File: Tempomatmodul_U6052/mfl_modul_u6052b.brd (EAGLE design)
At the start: 78 x 58 mm, 27 parts, among them IC1 U6052B-A, J1 43045-0800, K1 APF30212C, K2 APF30212C, K3 APF30212C, K4 APF30212C

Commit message: Fixed. Running version!
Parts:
- removed D6: P6KEXXC, diode:CB417-15
- removed R11, R12: 665, rcl:0207/7
- removed R13: 931, rcl:0207/7
- added C3: 100nF, rcl:C025-025X050
- added LED1: led grün 2,2v 20mA, led:LED3MM
- C1: value 100µF -> 1nF
- C2: value 1nF -> 100uF/36V; device rcl:C025-025X050 -> rcl:E2,5-6
- D1: value BYW52 -> EP20D; device diode:DO204-10 -> diode:DO15-12
- D2, D3, D4, D5: value CGRM4004-G -> MBSR140; device diode:SOD-123_MINI-SMA -> Heinrich:DO214AA
- J1: value 43045-0800 -> 39-30-1100; device Heinrich:43045-0800 -> Heinrich:39-30-1100
- R1: value 100 -> 560
- R10: value 200 -> 510
- R2: value 510 -> 100
- R3: value 200 -> 200k
- R4: value 270k -> 200
- R5: value 20k -> 931
- R6: value 150k -> 665
- R7: value 39k -> 665
- R8: value 200k -> 200
- R9: value 66.5 -> 66,5
- moved R8 67.8 mm to (69.8, 51.4), turned to 90 degrees
- moved R10 53.2 mm to (33.0, 16.5), turned to 0 degrees
- moved R3 44.2 mm to (56.5, 7.62), turned to 0 degrees
- moved R1 41.3 mm to (69.8, 17.8), turned to 90 degrees
- moved R5 38.1 mm to (39.4, 44.5), turned to 270 degrees
- moved R7 33.9 mm to (47.0, 51.4), turned to 90 degrees
- moved R6 32.0 mm to (62.2, 51.4), turned to 90 degrees
- moved C1 31.8 mm to (54.6, 23.5), turned to 0 degrees
- moved R4 27.6 mm to (33.0, 9.53), turned to 0 degrees
- moved R2 23.9 mm to (45.7, 23.5), turned to 0 degrees
- moved IC1 21.9 mm to (50.8, 16.5), turned to 180 degrees
- moved D1 14.9 mm to (24.8, 24.8), turned to 270 degrees
- moved C2 11.7 mm to (33.0, 22.2), turned to 180 degrees
- moved R9 11.4 mm to (54.6, 51.4)
- moved J1 6.35 mm to (0.00, 33.0)
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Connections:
- net K1 renamed PLUS
- net K2 renamed ABRUF
- net K3 renamed MINUS
- net K4 renamed I/O
- removed net +12V: D1.C, D2.C, D3.C, D4.C, D5.C, K1.2, K2.2, K3.2, K4.2, R2.1, R3.1, R4.1, R6.1
- removed net LD: IC1.15, R4.2, R5.2
- removed net MFL_CC: J1.5, R1.1
- removed net N$6: K1.NO, K2.NO, K3.NO, K4.NC, R11.1, R13.2
- removed net N$8: K2.COM, R10.1
- removed net PO: IC1.3, R6.2, R7.2
- new net IBUS: J1.3, J1.4
- new net MFL: J1.6, R2.1
- new net N$10: K2.COM, R8.1
- new net N$11: K3.COM, R7.1
- new net N$12: K1.NO, K2.NO, K3.NO, K4.NC, R5.2, R6.1
- new net N$3: LED1.A, R1.1
- new net VCC: D1.C, D2.C, D3.C, D4.C, D5.C, K1.2, K2.2, K3.2, K4.2, R1.2, R10.1, R4.1
- net EML1: now also J1.5, R6.2, R7.2, R8.2; no longer J1.8, R10.2, R11.2, R12.2
- net EML2: now also J1.10, R5.1; no longer J1.4, R13.1
- net GND: now also C2.-, C3.2, IC1.15, IC1.3, J1.7, J1.8, J1.9; no longer C2.2, D6.A, J1.2, J1.3, R5.1, R7.1
- net N$1: now also R2.2; no longer R1.2
- net N$2: now also R4.2; no longer R3.2
- net N$4: now also IC1.18, LED1.K; no longer K3.COM, R12.1
- net OSC: now also C1.1, R3.2; no longer C2.1, R8.2
- net VBAT: now also J1.1, J1.2; no longer D6.C, J1.6, J1.7
- net VS: now also C2.+, C3.1, R10.2; no longer C1.1, R2.2
- net VSTAB: now also R3.1; no longer R8.1
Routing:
- net VCC: track 0.00 -> 123.5 mm
- net +12V: track 104.3 -> 0.00 mm
- net N$12: track 0.00 -> 39.6 mm
- net ABRUF: track 49.7 -> 12.1 mm
- net LD: track 35.0 -> 0.00 mm, vias 1 -> 0
- net N$6: track 34.5 -> 0.00 mm
- net PLUS: track 41.7 -> 9.04 mm
- net MFL: track 0.00 -> 23.0 mm
- net PO: track 21.8 -> 0.00 mm
- net MINUS: track 42.3 -> 20.7 mm
- net MFL_CC: track 17.4 -> 0.00 mm
- net I/O: track 26.5 -> 9.45 mm
- net N$2: track 27.7 -> 11.7 mm
- net EML2: track 45.4 -> 29.8 mm, vias 1 -> 0
- net VBAT: track 12.7 -> 20.5 mm
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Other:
- board text added: "BMW MFL Dekoder für BMW E31 / M70 Heinrich Geiger für www.8er.org"
- board text removed: "8-Bit MFL Dekoder für BMW E31 / M70 Heinrich Geiger (c) www.8er.org"

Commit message: Fosc corrected
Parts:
- C1: value 1nF -> 680pF
- R3: value 200k -> 69k6
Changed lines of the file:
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@@
 </autorouter>
 <elements>
-<element name="C1" library="rcl" library_urn="urn:adsk.eagle:library:334" package="C025-025X050" package3d_urn="urn:adsk.eagle:package:23629/2" value="1nF" x="54.61" y="23.495" smashed="yes">
+<element name="C1" library="rcl" library_urn="urn:adsk.eagle:library:334" package="C025-025X050" package3d_urn="urn:adsk.eagle:package:23629/2" value="680pF" x="54.61" y="23.495" smashed="yes">
 <attribute name="NAME" x="58.801" y="22.479" size="1.27" layer="25" font="vector" ratio="15" rot="R90"/>
 <attribute name="SPICEPREFIX" value="C" x="54.61" y="23.495" size="1.778" layer="27" display="off"/>
@@
 <attribute name="SPICEPREFIX" value="R" x="45.72" y="23.495" size="1.778" layer="27" display="off"/>
 </element>
-<element name="R3" library="rcl" library_urn="urn:adsk.eagle:library:334" package="0207/7" package3d_urn="urn:adsk.eagle:package:23493/1" value="200k" x="56.515" y="7.62" smashed="yes">
+<element name="R3" library="rcl" library_urn="urn:adsk.eagle:library:334" package="0207/7" package3d_urn="urn:adsk.eagle:package:23493/1" value="69k6" x="56.515" y="7.62" smashed="yes">
 <attribute name="NAME" x="62.738" y="6.35" size="1.27" layer="25" font="vector" ratio="15" rot="R90"/>
 <attribute name="SPICEPREFIX" value="R" x="56.515" y="7.62" size="1.778" layer="27" display="off"/>

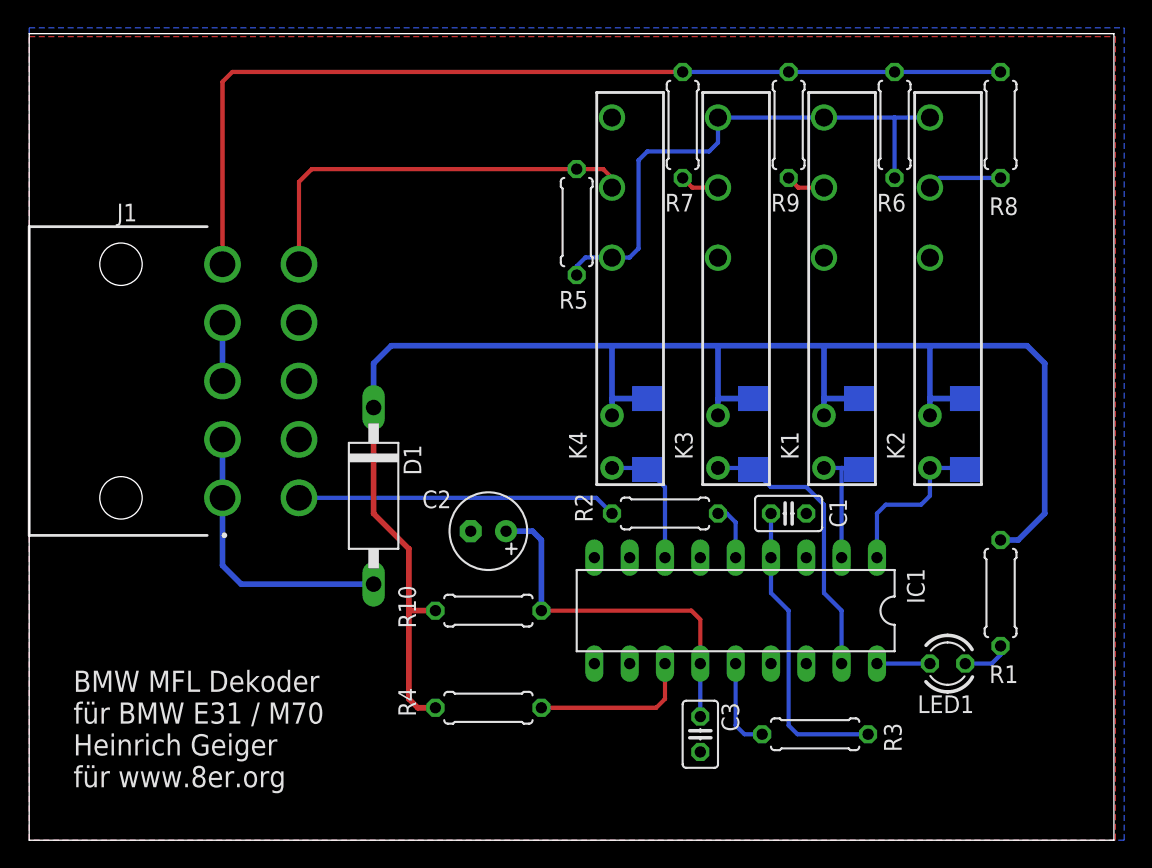
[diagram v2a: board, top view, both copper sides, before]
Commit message: Added support for V8 engines (M60 and M62)
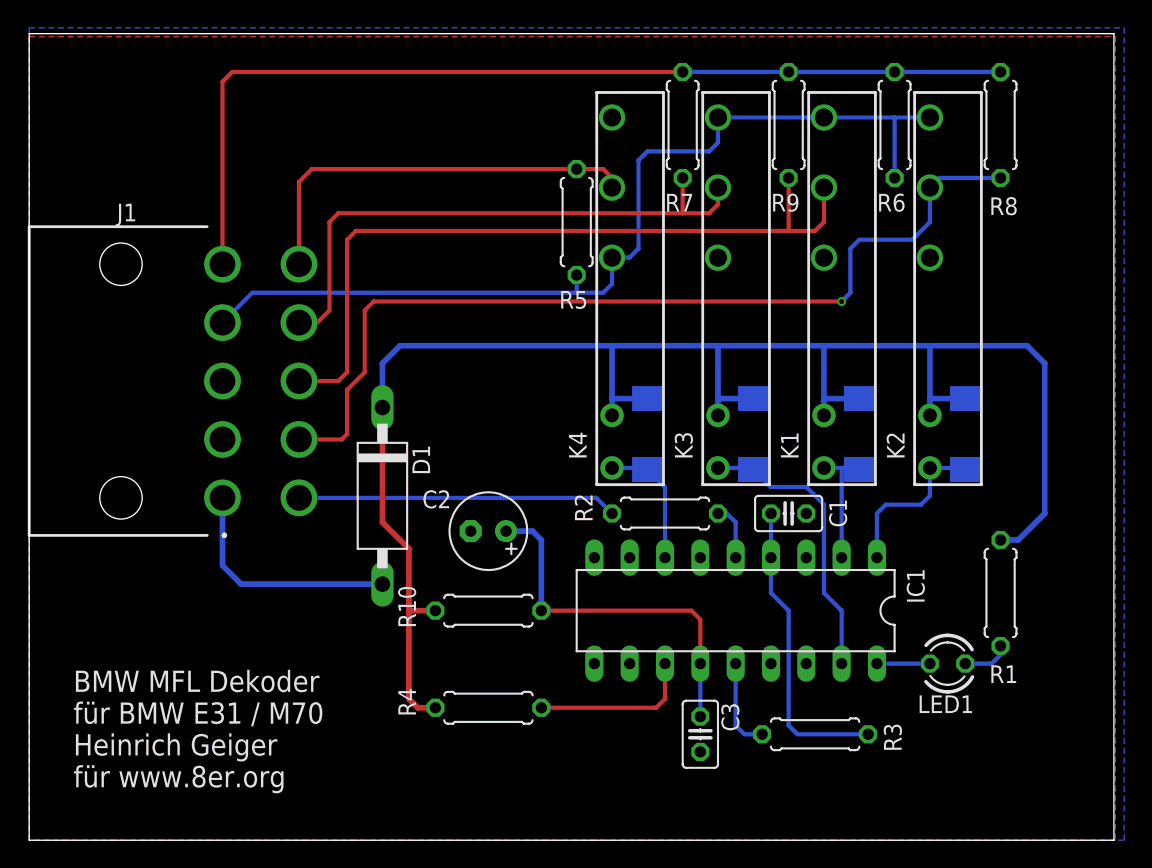
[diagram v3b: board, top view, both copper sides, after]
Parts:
- moved D1 0.63 mm to (25.4, 24.8)
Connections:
- net EML2 renamed EML2/X72.4
- removed net IBUS: J1.3, J1.4
- removed net N$10: K2.COM, R8.1
- removed net N$11: K3.COM, R7.1
- removed net N$12: K1.NO, K2.NO, K3.NO, K4.NC, R5.2, R6.1
- removed net N$9: K1.COM, R9.1
- new net X72.1: J1.4, K1.NO, K2.NO, K3.NO, K4.NC, R5.2, R6.1
- new net X72.2: J1.7, K2.COM, R8.1
- new net X72.3: J1.9, K3.COM, R7.1
- new net X72.7: J1.8, K1.COM, R9.1
- net GND: now also J1.2; no longer J1.7, J1.8, J1.9
- net VBAT: no longer J1.2
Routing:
- net X72.1: track 0.00 -> 68.5 mm
- net X72.2: track 0.00 -> 66.0 mm, vias 0 -> 1
- net X72.7: track 0.00 -> 54.4 mm
- net X72.3: track 0.00 -> 41.1 mm
- net N$12: track 39.6 -> 0.00 mm
- net N$10: track 5.37 -> 0.00 mm
- net IBUS: track 4.20 -> 0.00 mm
- net VBAT: track 20.5 -> 16.9 mm
- net N$9: track 2.83 -> 0.00 mm
- net N$11: track 2.83 -> 0.00 mm
- net VCC: track 123.5 -> 122.6 mm
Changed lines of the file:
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@@
 <attribute name="SPICEPREFIX" value="C" x="33.02" y="22.225" size="1.778" layer="27" rot="R180" display="off"/>
 </element>
-<element name="D1" library="diode" library_urn="urn:adsk.eagle:library:210" package="DO15-12" package3d_urn="urn:adsk.eagle:package:43369/1" value="EP20D" x="24.765" y="24.765" smashed="yes" rot="R270">
-<attribute name="NAME" x="26.924" y="28.448" size="1.27" layer="25" font="vector" ratio="15" rot="R270"/>
+<element name="D1" library="diode" library_urn="urn:adsk.eagle:library:210" package="DO15-12" package3d_urn="urn:adsk.eagle:package:43369/1" value="EP20D" x="25.4" y="24.765" smashed="yes" rot="R270">
+<attribute name="NAME" x="27.559" y="28.448" size="1.27" layer="25" font="vector" ratio="15" rot="R270"/>
 </element>
 <element name="D2" library="Heinrich" package="DO214AA" value="MBSR140" x="59.69" y="29.21" smashed="yes" rot="MR270">
@@
 <vertex x="0" y="0"/>
 </polygon>
-<contactref element="J1" pad="7"/>
-<contactref element="J1" pad="9"/>
-<contactref element="J1" pad="8"/>
 <contactref element="C3" pad="2"/>
+<contactref element="J1" pad="2"/>
 </signal>
 <signal name="N$1">
@@
 <contactref element="K4" pad="2"/>
 <contactref element="R1" pad="2"/>
-<wire x1="24.765" y1="31.115" x2="24.765" y2="34.29" width="0.4064" layer="16"/>
-<wire x1="24.765" y1="34.29" x2="26.035" y2="35.56" width="0.4064" layer="16"/>
+<wire x1="25.4" y1="31.115" x2="25.4" y2="34.29" width="0.4064" layer="16"/>
+<wire x1="25.4" y1="34.29" x2="26.67" y2="35.56" width="0.4064" layer="16"/>
 <wire x1="71.755" y1="35.56" x2="73.025" y2="34.29" width="0.4064" layer="16"/>
-<wire x1="26.035" y1="35.56" x2="41.91" y2="35.56" width="0.4064" layer="16"/>
+<wire x1="26.67" y1="35.56" x2="41.91" y2="35.56" width="0.4064" layer="16"/>
 <wire x1="41.91" y1="35.56" x2="49.53" y2="35.56" width="0.4064" layer="16"/>
 <wire x1="49.53" y1="35.56" x2="57.15" y2="35.56" width="0.4064" layer="16"/>
@@
 <wire x1="64.78" y1="31.76" x2="64.77" y2="31.75" width="0.4064" layer="16"/>
 <wire x1="73.025" y1="34.29" x2="73.025" y2="23.495" width="0.4064" layer="16"/>
-<wire x1="24.765" y1="31.115" x2="24.765" y2="23.495" width="0.4064" layer="1"/>
+<wire x1="25.4" y1="31.115" x2="25.4" y2="22.86" width="0.4064" layer="1"/>
 <wire x1="27.305" y1="20.955" x2="27.305" y2="16.51" width="0.4064" layer="1"/>
-<wire x1="24.765" y1="23.495" x2="27.305" y2="20.955" width="0.4064" layer="1"/>
+<wire x1="25.4" y1="22.86" x2="27.305" y2="20.955" width="0.4064" layer="1"/>
 <wire x1="29.21" y1="16.51" x2="27.305" y2="16.51" width="0.4064" layer="1"/>
 <wire x1="27.305" y1="10.16" x2="27.94" y2="9.525" width="0.4064" layer="1"/>
@@
 <contactref element="D1" pad="A"/>
 <contactref element="J1" pad="1"/>
-<contactref element="J1" pad="2"/>
 <wire x1="13.9" y1="24.62" x2="13.9" y2="19.755" width="0.4064" layer="16"/>
 <wire x1="13.9" y1="19.755" x2="15.24" y2="18.415" width="0.4064" layer="16"/>
-<wire x1="15.24" y1="18.415" x2="24.765" y2="18.415" width="0.4064" layer="16"/>
-<wire x1="13.9" y1="24.62" x2="13.9" y2="28.82" width="0.4064" layer="16"/>
+<wire x1="15.24" y1="18.415" x2="25.4" y2="18.415" width="0.4064" layer="16"/>
 </signal>
 <signal name="MFL">
@@
 <wire x1="14.605" y1="55.245" x2="46.99" y2="55.245" width="0.3048" layer="1"/>
 </signal>
-<signal name="N$9">
+<signal name="X72.7">
 <contactref element="R9" pad="1"/>
 <contactref element="K1" pad="COM"/>
-<wire x1="57.15" y1="46.93" x2="55.305" y2="46.93" width="0.3048" layer="1"/>
-<wire x1="55.305" y1="46.93" x2="54.61" y2="47.625" width="0.3048" layer="1"/>
-</signal>
-<signal name="N$10">
+<contactref element="J1" pad="8"/>
+<wire x1="22.225" y1="33.02" x2="22.86" y2="33.655" width="0.3048" layer="1"/>
+<wire x1="22.86" y1="33.655" x2="22.86" y2="43.18" width="0.3048" layer="1"/>
+<wire x1="22.86" y1="43.18" x2="23.495" y2="43.815" width="0.3048" layer="1"/>
+<wire x1="23.495" y1="43.815" x2="54.61" y2="43.815" width="0.3048" layer="1"/>
+<wire x1="54.61" y1="43.815" x2="56.515" y2="43.815" width="0.3048" layer="1"/>
+<wire x1="56.515" y1="43.815" x2="57.15" y2="44.45" width="0.3048" layer="1"/>
+<wire x1="57.15" y1="44.45" x2="57.15" y2="46.93" width="0.3048" layer="1"/>
+<wire x1="19.4" y1="33.02" x2="22.225" y2="33.02" width="0.3048" layer="1"/>
+<wire x1="54.61" y1="47.625" x2="54.61" y2="43.815" width="0.3048" layer="1"/>
+</signal>
+<signal name="X72.2">
 <contactref element="R8" pad="1"/>
 <contactref element="K2" pad="COM"/>
 <wire x1="69.85" y1="47.625" x2="65.465" y2="47.625" width="0.3048" layer="16"/>
 <wire x1="65.465" y1="47.625" x2="64.77" y2="46.93" width="0.3048" layer="16"/>
-</signal>
-<signal name="N$11">
-<contactref element="R7" pad="1"/>
-<contactref element="K3" pad="COM"/>
-<wire x1="49.53" y1="46.93" x2="47.685" y2="46.93" width="0.3048" layer="1"/>
-<wire x1="47.685" y1="46.93" x2="46.99" y2="47.625" width="0.3048" layer="1"/>
-</signal>
-<signal name="N$12">
+<contactref element="J1" pad="7"/>
+<wire x1="64.77" y1="46.93" x2="64.77" y2="44.45" width="0.3048" layer="16"/>
+<wire x1="64.77" y1="44.45" x2="63.5" y2="43.18" width="0.3048" layer="16"/>
+<wire x1="63.5" y1="43.18" x2="59.69" y2="43.18" width="0.3048" layer="16"/>
+<wire x1="59.69" y1="43.18" x2="59.055" y2="42.545" width="0.3048" layer="16"/>
+<wire x1="59.055" y1="42.545" x2="59.055" y2="39.37" width="0.3048" layer="16"/>
+<wire x1="59.055" y1="39.37" x2="58.42" y2="38.735" width="0.3048" layer="16"/>
+<wire x1="19.4" y1="28.82" x2="22.47" y2="28.82" width="0.3048" layer="1"/>
+<wire x1="22.47" y1="28.82" x2="22.86" y2="29.21" width="0.3048" layer="1"/>
+<wire x1="22.86" y1="29.21" x2="22.86" y2="32.385" width="0.3048" layer="1"/>
+<wire x1="24.13" y1="33.655" x2="24.13" y2="38.1" width="0.3048" layer="1"/>
+<wire x1="24.13" y1="38.1" x2="24.765" y2="38.735" width="0.3048" layer="1"/>
+<wire x1="22.86" y1="32.385" x2="24.13" y2="33.655" width="0.3048" layer="1"/>
+<wire x1="24.765" y1="38.735" x2="58.42" y2="38.735" width="0.3048" layer="1"/>
+<via x="58.42" y="38.735" extent="1-16" drill="0.35"/>
+</signal>
+<signal name="X72.1">
 <contactref element="R6" pad="1"/>
 <contactref element="R5" pad="2"/>
@@
 <wire x1="41.91" y1="41.89" x2="41.9" y2="41.9" width="0.3048" layer="16"/>
 <wire x1="41.9" y1="41.9" x2="41.89" y2="41.91" width="0.3048" layer="16"/>
-<wire x1="41.89" y1="41.91" x2="40.005" y2="41.91" width="0.3048" layer="16"/>
-<wire x1="40.005" y1="41.91" x2="39.37" y2="41.275" width="0.3048" layer="16"/>
-<wire x1="39.37" y1="41.275" x2="39.37" y2="40.64" width="0.3048" layer="16"/>
 <wire x1="49.53" y1="51.97" x2="49.53" y2="50.165" width="0.3048" layer="16"/>
 <wire x1="49.53" y1="50.165" x2="48.895" y2="49.53" width="0.3048" layer="16"/>
@@
 <wire x1="62.23" y1="51.97" x2="64.77" y2="51.97" width="0.3048" layer="16"/>
 <wire x1="62.23" y1="47.625" x2="62.23" y2="51.97" width="0.3048" layer="16"/>
-</signal>
-<signal name="EML2">
-<contactref element="R5" pad="1"/>
-<contactref element="K4" pad="COM"/>
-<contactref element="J1" pad="10"/>
-<wire x1="20.32" y1="48.26" x2="39.37" y2="48.26" width="0.3048" layer="1"/>
-<wire x1="19.4" y1="41.42" x2="19.4" y2="47.34" width="0.3048" layer="1"/>
-<wire x1="19.4" y1="47.34" x2="20.32" y2="48.26" width="0.3048" layer="1"/>
-<wire x1="39.37" y1="48.26" x2="41.275" y2="48.26" width="0.3048" layer="1"/>
-<wire x1="41.275" y1="48.26" x2="41.91" y2="47.625" width="0.3048" layer="1"/>
-<wire x1="41.91" y1="47.625" x2="41.91" y2="46.93" width="0.3048" layer="1"/>
-</signal>
-<signal name="IBUS">
-<contactref element="J1" pad="3"/>
 <contactref element="J1" pad="4"/>
-<wire x1="13.9" y1="33.02" x2="13.9" y2="37.22" width="0.4064" layer="16"/>
+<wire x1="13.9" y1="37.22" x2="16.05" y2="39.37" width="0.3048" layer="16"/>
+<wire x1="41.275" y1="39.37" x2="41.91" y2="40.005" width="0.3048" layer="16"/>
+<wire x1="41.91" y1="40.005" x2="41.91" y2="41.89" width="0.3048" layer="16"/>
+<wire x1="16.05" y1="39.37" x2="39.37" y2="39.37" width="0.3048" layer="16"/>
+<wire x1="39.37" y1="39.37" x2="41.275" y2="39.37" width="0.3048" layer="16"/>
+<wire x1="39.37" y1="40.64" x2="39.37" y2="39.37" width="0.3048" layer="16"/>
 </signal>
 <signal name="N$3">
@@
 <wire x1="60.96" y1="12.7" x2="64.77" y2="12.7" width="0.3048" layer="16"/>
 </signal>
+<signal name="X72.3">
+<contactref element="K3" pad="COM"/>
+<contactref element="R7" pad="1"/>
+<contactref element="J1" pad="9"/>
+<wire x1="19.4" y1="37.22" x2="20.71" y2="37.22" width="0.3048" layer="1"/>
+<wire x1="20.71" y1="37.22" x2="21.59" y2="38.1" width="0.3048" layer="1"/>
+<wire x1="21.59" y1="44.45" x2="21.59" y2="38.1" width="0.3048" layer="1"/>
+<wire x1="21.59" y1="44.45" x2="22.225" y2="45.085" width="0.3048" layer="1"/>
+<wire x1="48.895" y1="45.085" x2="49.53" y2="45.72" width="0.3048" layer="1"/>
+<wire x1="49.53" y1="45.72" x2="49.53" y2="46.93" width="0.3048" layer="1"/>
+<wire x1="22.225" y1="45.085" x2="46.99" y2="45.085" width="0.3048" layer="1"/>
+<wire x1="46.99" y1="45.085" x2="48.895" y2="45.085" width="0.3048" layer="1"/>
+<wire x1="46.99" y1="47.625" x2="46.99" y2="45.085" width="0.3048" layer="1"/>
+</signal>
+<signal name="EML2/X72.4">
+<contactref element="R5" pad="1"/>
+<contactref element="K4" pad="COM"/>
+<wire x1="39.37" y1="48.26" x2="41.275" y2="48.26" width="0.3048" layer="1"/>
+<wire x1="41.275" y1="48.26" x2="41.91" y2="47.625" width="0.3048" layer="1"/>
+<wire x1="41.91" y1="47.625" x2="41.91" y2="46.93" width="0.3048" layer="1"/>
+<contactref element="J1" pad="10"/>
+<wire x1="19.4" y1="41.42" x2="19.4" y2="47.34" width="0.3048" layer="1"/>
+<wire x1="19.4" y1="47.34" x2="20.32" y2="48.26" width="0.3048" layer="1"/>
+<wire x1="20.32" y1="48.26" x2="39.37" y2="48.26" width="0.3048" layer="1"/>
+</signal>
 </signals>

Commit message: refactoring
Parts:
- R3: value 69k6 -> 69k8
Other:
- board text added: "BMW MFL Dekoder für BMW E31 V8 und V12 Heinrich Geiger für www.8er.org"
- board text removed: "BMW MFL Dekoder für BMW E31 / M70 Heinrich Geiger für www.8er.org"
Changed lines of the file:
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@@
 <wire x1="0" y1="58" x2="0" y2="0" width="0" layer="20"/>
 <text x="3.175" y="3.81" size="1.524" layer="25" font="vector" ratio="15">BMW MFL Dekoder
-für BMW E31 / M70
+für BMW E31
+V8 und V12
 Heinrich Geiger
 für www.8er.org</text>
@@
 <attribute name="SPICEPREFIX" value="R" x="45.72" y="23.495" size="1.778" layer="27" display="off"/>
 </element>
-<element name="R3" library="rcl" library_urn="urn:adsk.eagle:library:334" package="0207/7" package3d_urn="urn:adsk.eagle:package:23493/1" value="69k6" x="56.515" y="7.62" smashed="yes">
+<element name="R3" library="rcl" library_urn="urn:adsk.eagle:library:334" package="0207/7" package3d_urn="urn:adsk.eagle:package:23493/1" value="69k8" x="56.515" y="7.62" smashed="yes">
 <attribute name="NAME" x="62.738" y="6.35" size="1.27" layer="25" font="vector" ratio="15" rot="R90"/>
 <attribute name="SPICEPREFIX" value="R" x="56.515" y="7.62" size="1.778" layer="27" display="off"/>
